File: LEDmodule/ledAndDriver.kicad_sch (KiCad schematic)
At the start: 0 parts

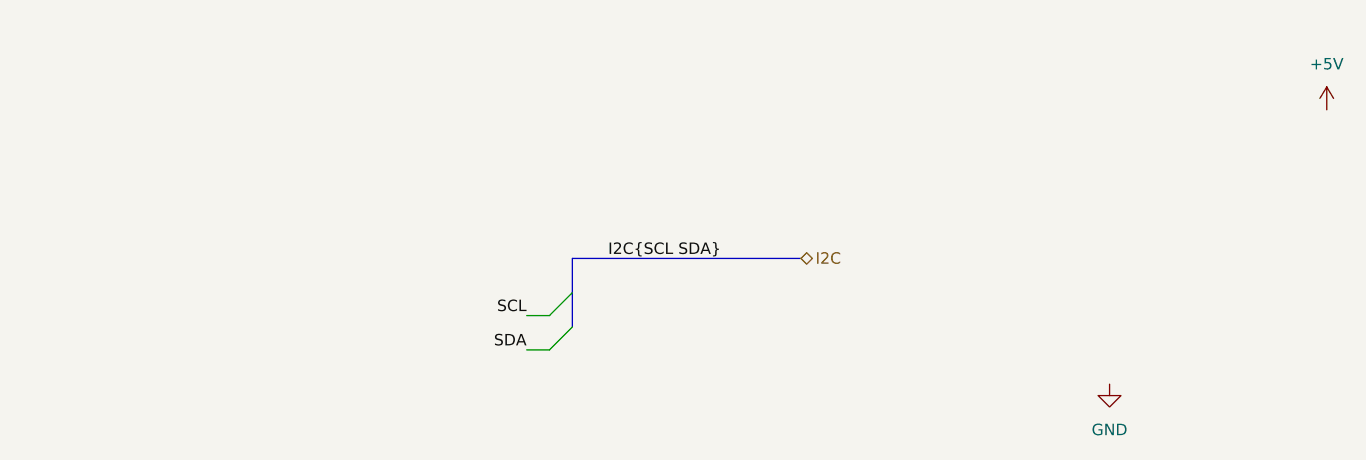
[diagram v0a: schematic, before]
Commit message: Add LP5012RUK symbol
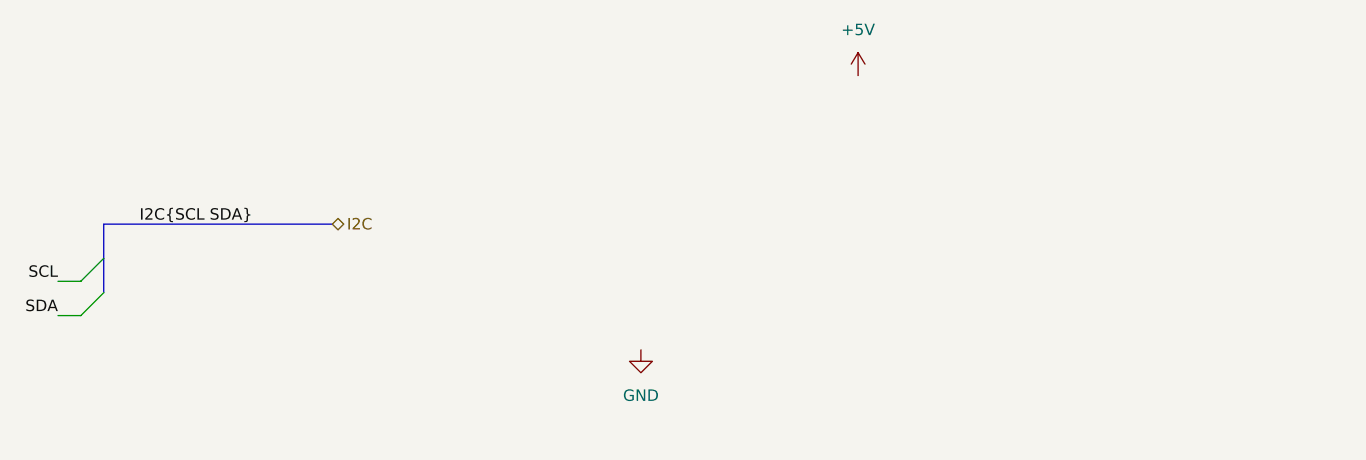
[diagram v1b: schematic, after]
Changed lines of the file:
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@@
 	)
 	(bus_entry
-		(at 124.46 86.36)
+		(at 72.39 82.55)
 		(size -2.54 2.54)
 		(stroke
@@
 	)
 	(bus_entry
-		(at 124.46 82.55)
+		(at 72.39 78.74)
 		(size -2.54 2.54)
 		(stroke
@@
 	(wire
 		(pts
-			(xy 119.38 85.09) (xy 121.92 85.09)
+			(xy 67.31 81.28) (xy 69.85 81.28)
 		)
 		(stroke
@@
 	(bus
 		(pts
-			(xy 124.46 78.74) (xy 124.46 82.55)
+			(xy 72.39 74.93) (xy 72.39 78.74)
 		)
 		(stroke
@@
 	(bus
 		(pts
-			(xy 124.46 78.74) (xy 149.86 78.74)
+			(xy 72.39 74.93) (xy 97.79 74.93)
 		)
 		(stroke
@@
 	(wire
 		(pts
-			(xy 119.38 88.9) (xy 121.92 88.9)
+			(xy 67.31 85.09) (xy 69.85 85.09)
 		)
 		(stroke
@@
 	(bus
 		(pts
-			(xy 124.46 82.55) (xy 124.46 86.36)
+			(xy 72.39 78.74) (xy 72.39 82.55)
 		)
 		(stroke
@@
 	)
 	(label "SDA"
-		(at 119.38 88.9 180)
+		(at 67.31 85.09 180)
 		(effects
 			(font
@@
 	)
 	(label "I2C{SCL SDA}"
-		(at 140.97 78.74 180)
+		(at 88.9 74.93 180)
 		(effects
 			(font
@@
 	)
 	(label "SCL"
-		(at 119.38 85.09 180)
+		(at 67.31 81.28 180)
 		(effects
 			(font
@@
 	(hierarchical_label "I2C"
 		(shape bidirectional)
-		(at 149.86 78.74 0)
+		(at 97.79 74.93 0)
 		(effects
 			(font
@@
 	(symbol
 		(lib_id "power:+5V")
-		(at 208.28 62.23 0)
+		(at 156.21 58.42 0)
 		(unit 1)
 		(exclude_from_sim no)
@@
 		(fields_autoplaced yes)
 		(property "Reference" "#PWR04"
-			(at 208.28 66.04 0)
+			(at 156.21 62.23 0)
 			(effects
 				(font
@@
 		)
 		(property "Value" "+5V"
-			(at 208.28 57.15 0)
+			(at 156.21 53.34 0)
 			(effects
 				(font
@@
 		)
 		(property "Footprint" ""
-			(at 208.28 62.23 0)
+			(at 156.21 58.42 0)
 			(effects
 				(font
@@
 		)
 		(property "Datasheet" ""
-			(at 208.28 62.23 0)
+			(at 156.21 58.42 0)
 			(effects
 				(font
@@
 		)
 		(property "Description" "Power symbol creates a global label with name \"+5V\""
-			(at 208.28 62.23 0)
+			(at 156.21 58.42 0)
 			(effects
 				(font
@@
 	(symbol
 		(lib_id "power:GND")
-		(at 184.15 92.71 0)
+		(at 132.08 88.9 0)
 		(unit 1)
 		(exclude_from_sim no)
@@
 		(fields_autoplaced yes)
 		(property "Reference" "#PWR03"
-			(at 184.15 99.06 0)
+			(at 132.08 95.25 0)
 			(effects
 				(font
@@
 		)
 		(property "Value" "GND"
-			(at 184.15 97.79 0)
+			(at 132.08 93.98 0)
 			(effects
 				(font
@@
 		)
 		(property "Footprint" ""
-			(at 184.15 92.71 0)
+			(at 132.08 88.9 0)
 			(effects
 				(font
@@
 		)
 		(property "Datasheet" ""
-			(at 184.15 92.71 0)
+			(at 132.08 88.9 0)
 			(effects
 				(font
@@
 		)
 		(property "Description" "Power symbol creates a global label with name \"GND\" , ground"
-			(at 184.15 92.71 0)
-			(effects
-				(font
+			(at 132.08 88.9 0)
+			(effects
+				(font

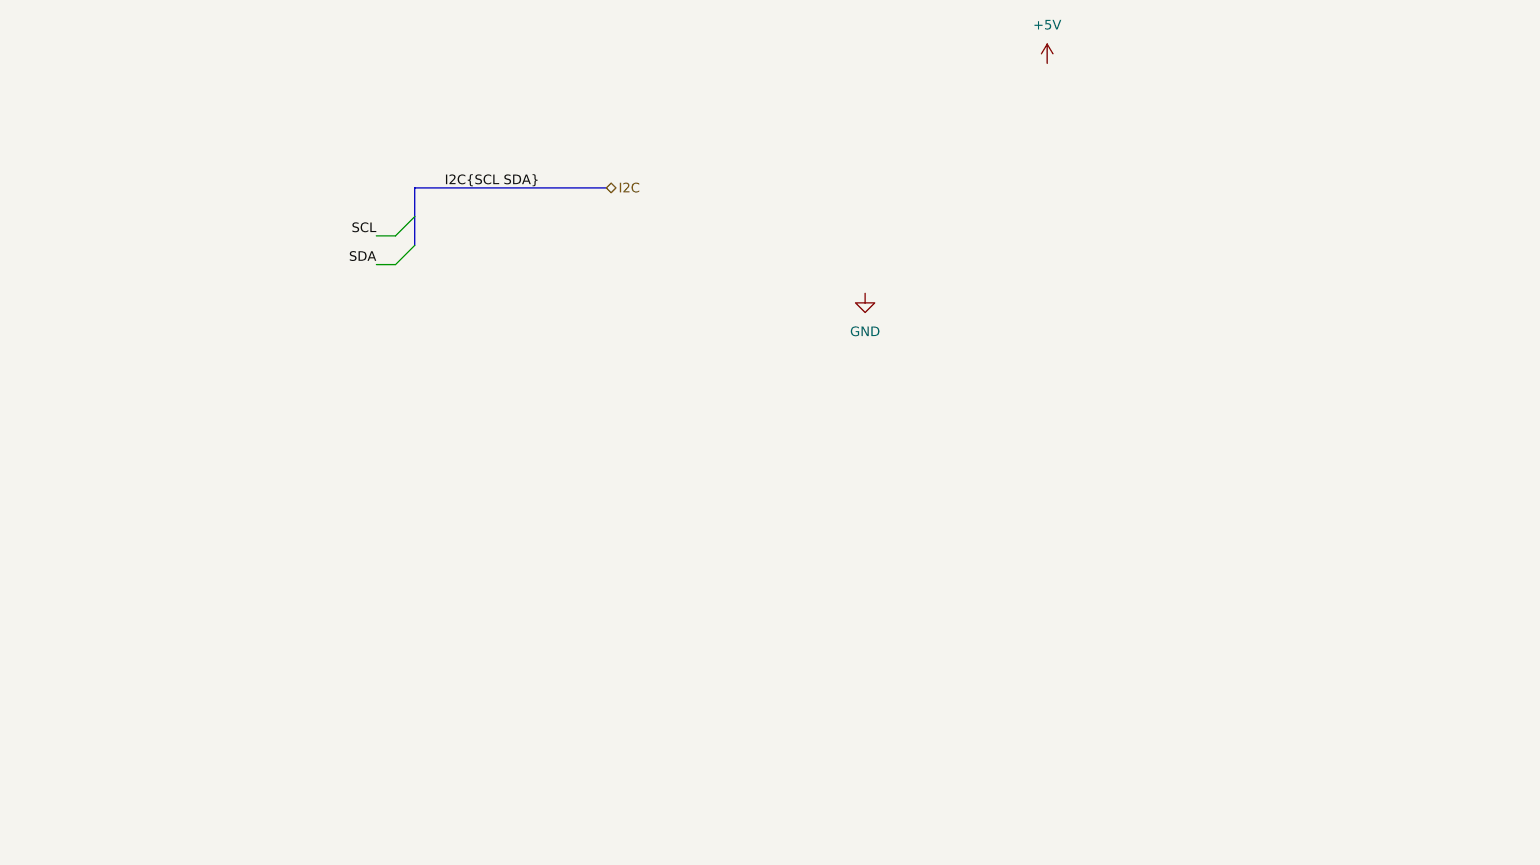
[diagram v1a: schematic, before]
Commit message: Added ledDriver without LED's
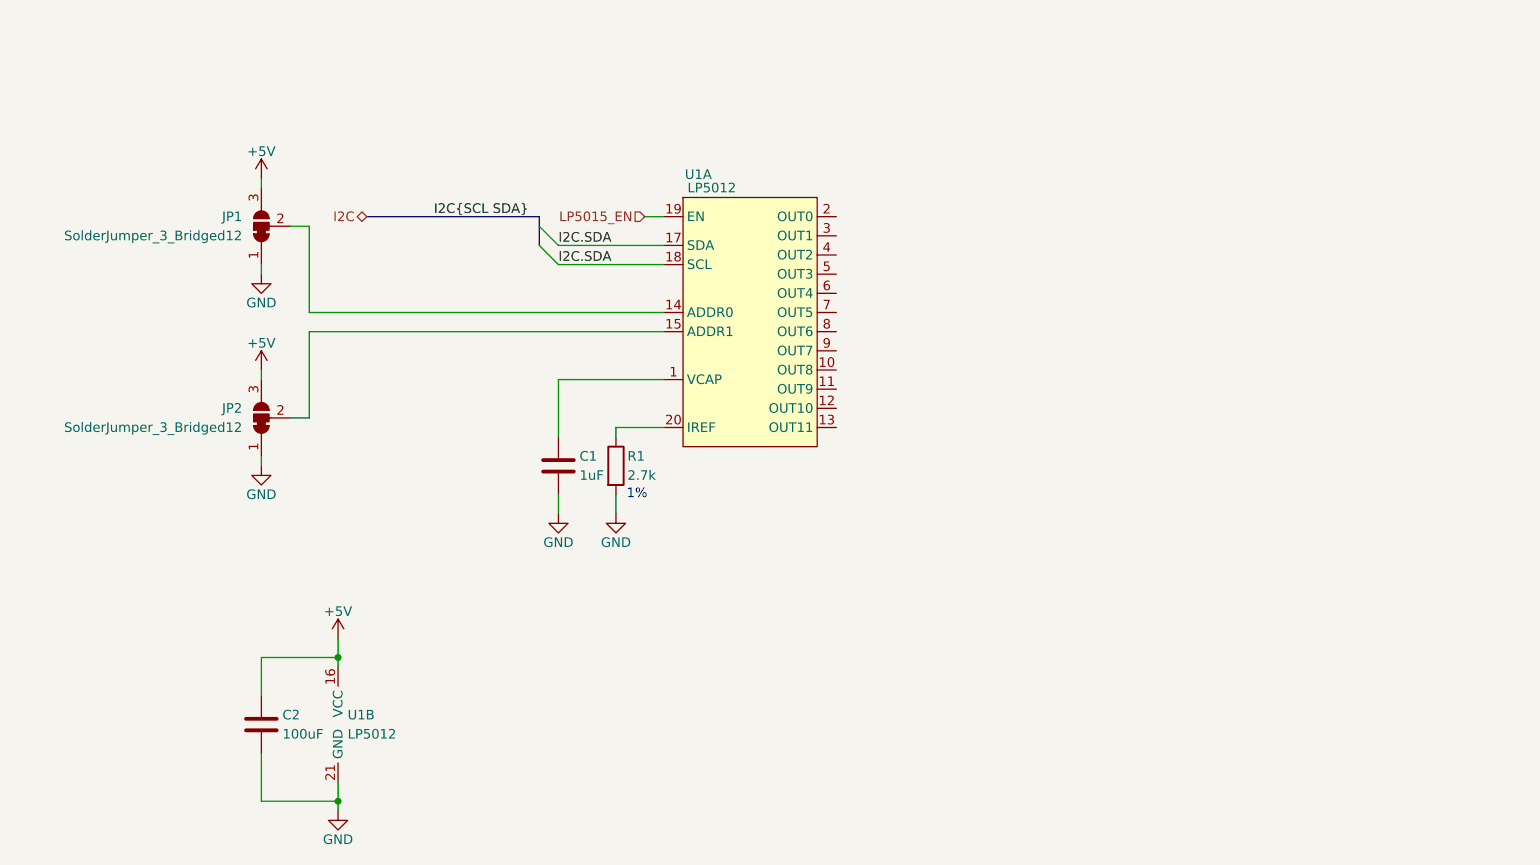
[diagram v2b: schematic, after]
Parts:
- added C1: 1uF, symbol Device:C
- added C2: 100uF, symbol Device:C
- added JP1, JP2: SolderJumper_3_Bridged12, symbol Jumper:SolderJumper_3_Bridged12
- added R1: 2.7k, symbol Device:R
- added U1: LP5012, symbol LP5012_ledDriver:LP5012RUK
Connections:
- net +5V: now also C2.1, JP1.3 (B), JP2.3 (B), U1.16 (VCC)
- net GND: now also C1.2, C2.2, JP1.1 (A), JP2.1 (A), R1.2, U1.21 (GND)
- new net: R1.1, U1.20 (IREF)
- new net: C1.1, U1.1 (VCAP)
- new net: JP2.2 (C), U1.15 (ADDR1)
- new net: JP1.2 (C), U1.14 (ADDR0)
- new net I2C.SDA: U1.17 (SDA), U1.18 (SCL)
- new net LP5015_EN: U1.19 (EN)
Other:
- note added: "1%"

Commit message: Finalize Led&Driver
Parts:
- added D2, D3, D4: RGBW LED, symbol LED_RGBW_GW-J9LHS2-4M:GW_J9LHS2.4M
- C1: value 1uF -> 1u
- C2: value 100uF -> 100n
- R1: value 2.7k -> 2k4
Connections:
- net +5V: now also D2.1, D2.2, D2.3, D2.4, D3.1, D3.2, D3.3, D3.4, D4.1, D4.2, D4.3, D4.4
- net at U1.10 (OUT8): now also D3.8
- net at U1.11 (OUT9): now also D4.6
- net at U1.12 (OUT10): now also D4.7
- net at U1.13 (OUT11): now also D4.8
- net at U1.2 (OUT0): now also D2.5
- net Cat_W2: now reaches U1.3 (OUT1)
- net Cat_W2: now also D3.5
- net Cat_W3: now reaches U1.4 (OUT2)
- net Cat_W3: now also D4.5
- net at U1.5 (OUT3): now also D2.6
- net at U1.6 (OUT4): now also D2.7
- net at U1.7 (OUT5): now also D2.8
- net at U1.8 (OUT6): now also D3.6
- net at U1.9 (OUT7): now also D3.7
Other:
- moved on the sheet: C1, C2, JP1, JP2, R1, U1A, U1B
